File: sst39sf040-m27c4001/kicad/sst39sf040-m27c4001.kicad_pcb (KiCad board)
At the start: 2 copper layers, 17.5 x 41.7 mm, 4 parts, among them J1 Conn_01x16_Male, J2 Conn_01x16_Male, SW1 SW_DPDT_x2, U1 SST39SF040

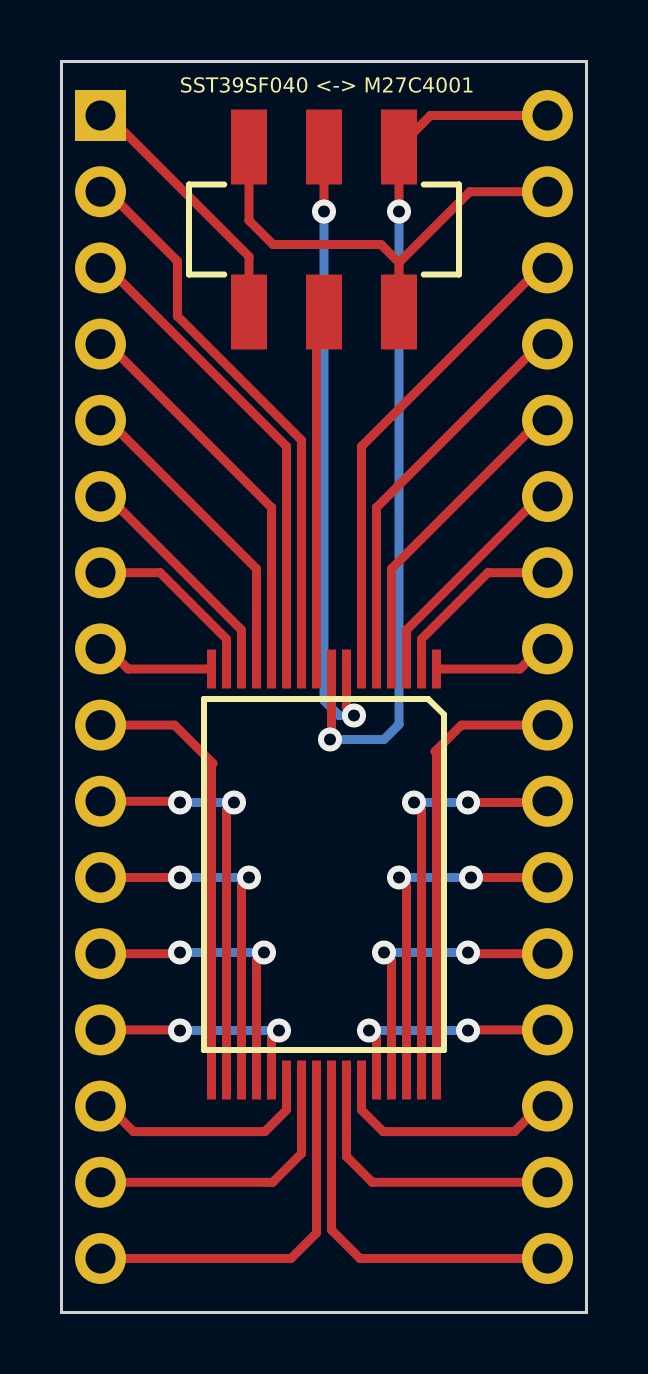
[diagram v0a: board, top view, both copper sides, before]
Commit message: fix wrong distance of pin row
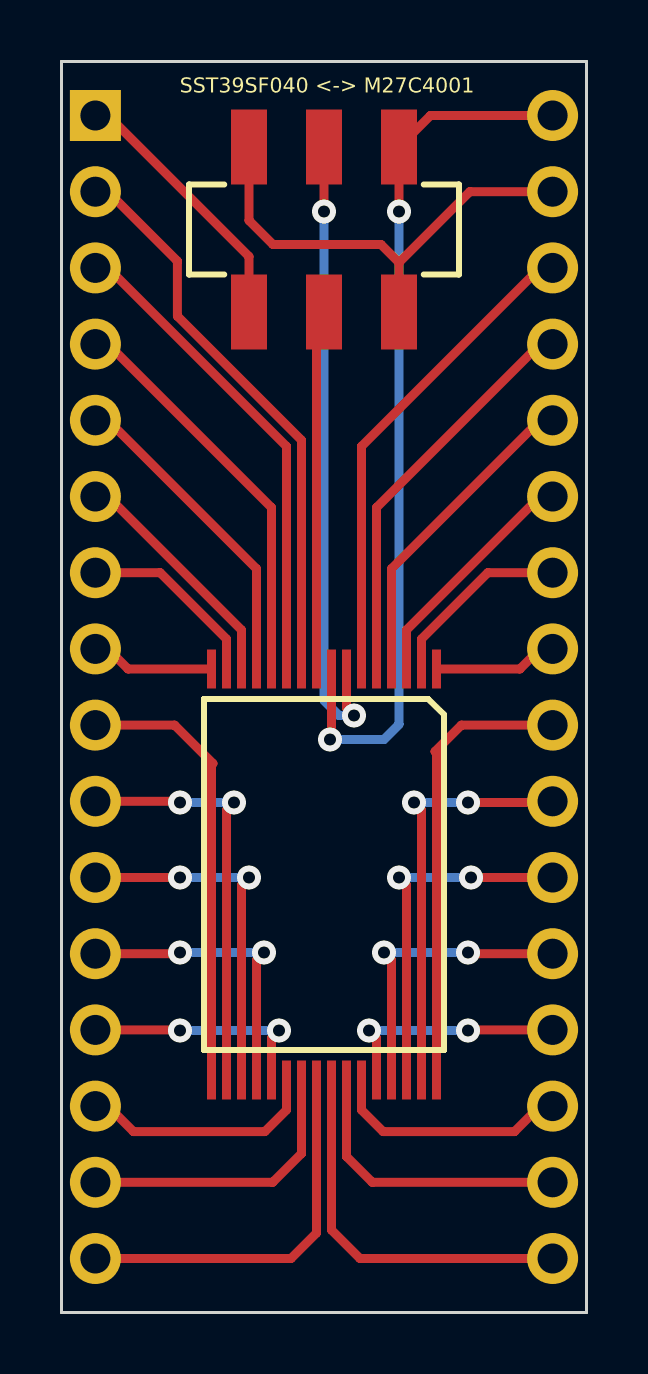
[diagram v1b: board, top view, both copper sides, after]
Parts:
- moved J2 0.17 mm to (140.6, 60.1)
- moved J1 0.17 mm to (125.4, 60.1)
